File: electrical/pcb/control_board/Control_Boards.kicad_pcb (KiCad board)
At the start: 2 copper layers, 220 x 367.6 mm, 141 parts, among them J1 XT30-M, J10 Molex_172675-0613, J11 Molex_172675-0613, J13 Molex_172675-0613, J14 Molex_172675-0613, J16 277-11404-ND, J17 277-11404-ND, J18 277-11404-ND, J19 TSW-104-07-F-T, J2 ED2580-ND, J20 PEC08SAAN, J21 PPTC102LFBN-RC, J22 S9175-ND_rpi_breakout, J23 S9175-ND_rpi_breakout, J24 6posheader, J25 SSW-104-01-F-T, J26 WM6548-ND, J27 PPTC021LFBN-RC, J28 PPTC021LFBN-RC, J29 PPTC021LFBN-RC, J3 XT30-F, J30 PEC08SAAN, J4 XT30-F, J5 XT30-M, J6 ED2580-ND, J8 Molex_172675-0613, J9 Molex_172675-0613, M1 Mounting_Holes, Q1 2N3906, Q2 2N3906, Q3 2N3906, Q4 2N3906, Q5 2N3906, Q6 2N3906, SW1 CT206124-ND, T1 test_point, T10 test_point, T11 test_point, T12 test_point, T13 test_point, T14 test_point, T15 test_point, T2 test_point, T3 test_point, T4 test_point, T5 test_point, T6 test_point, T7 test_point, T8 test_point, T9 test_point, U1 INA260, U2 PCA9685, U3 D24V22Fx, U4 D24V150Fx, U5 DC7G3HWA, U6 DC7G3HWA, U7 MIC2937A-3.3WT, y1 rover_silkscreen

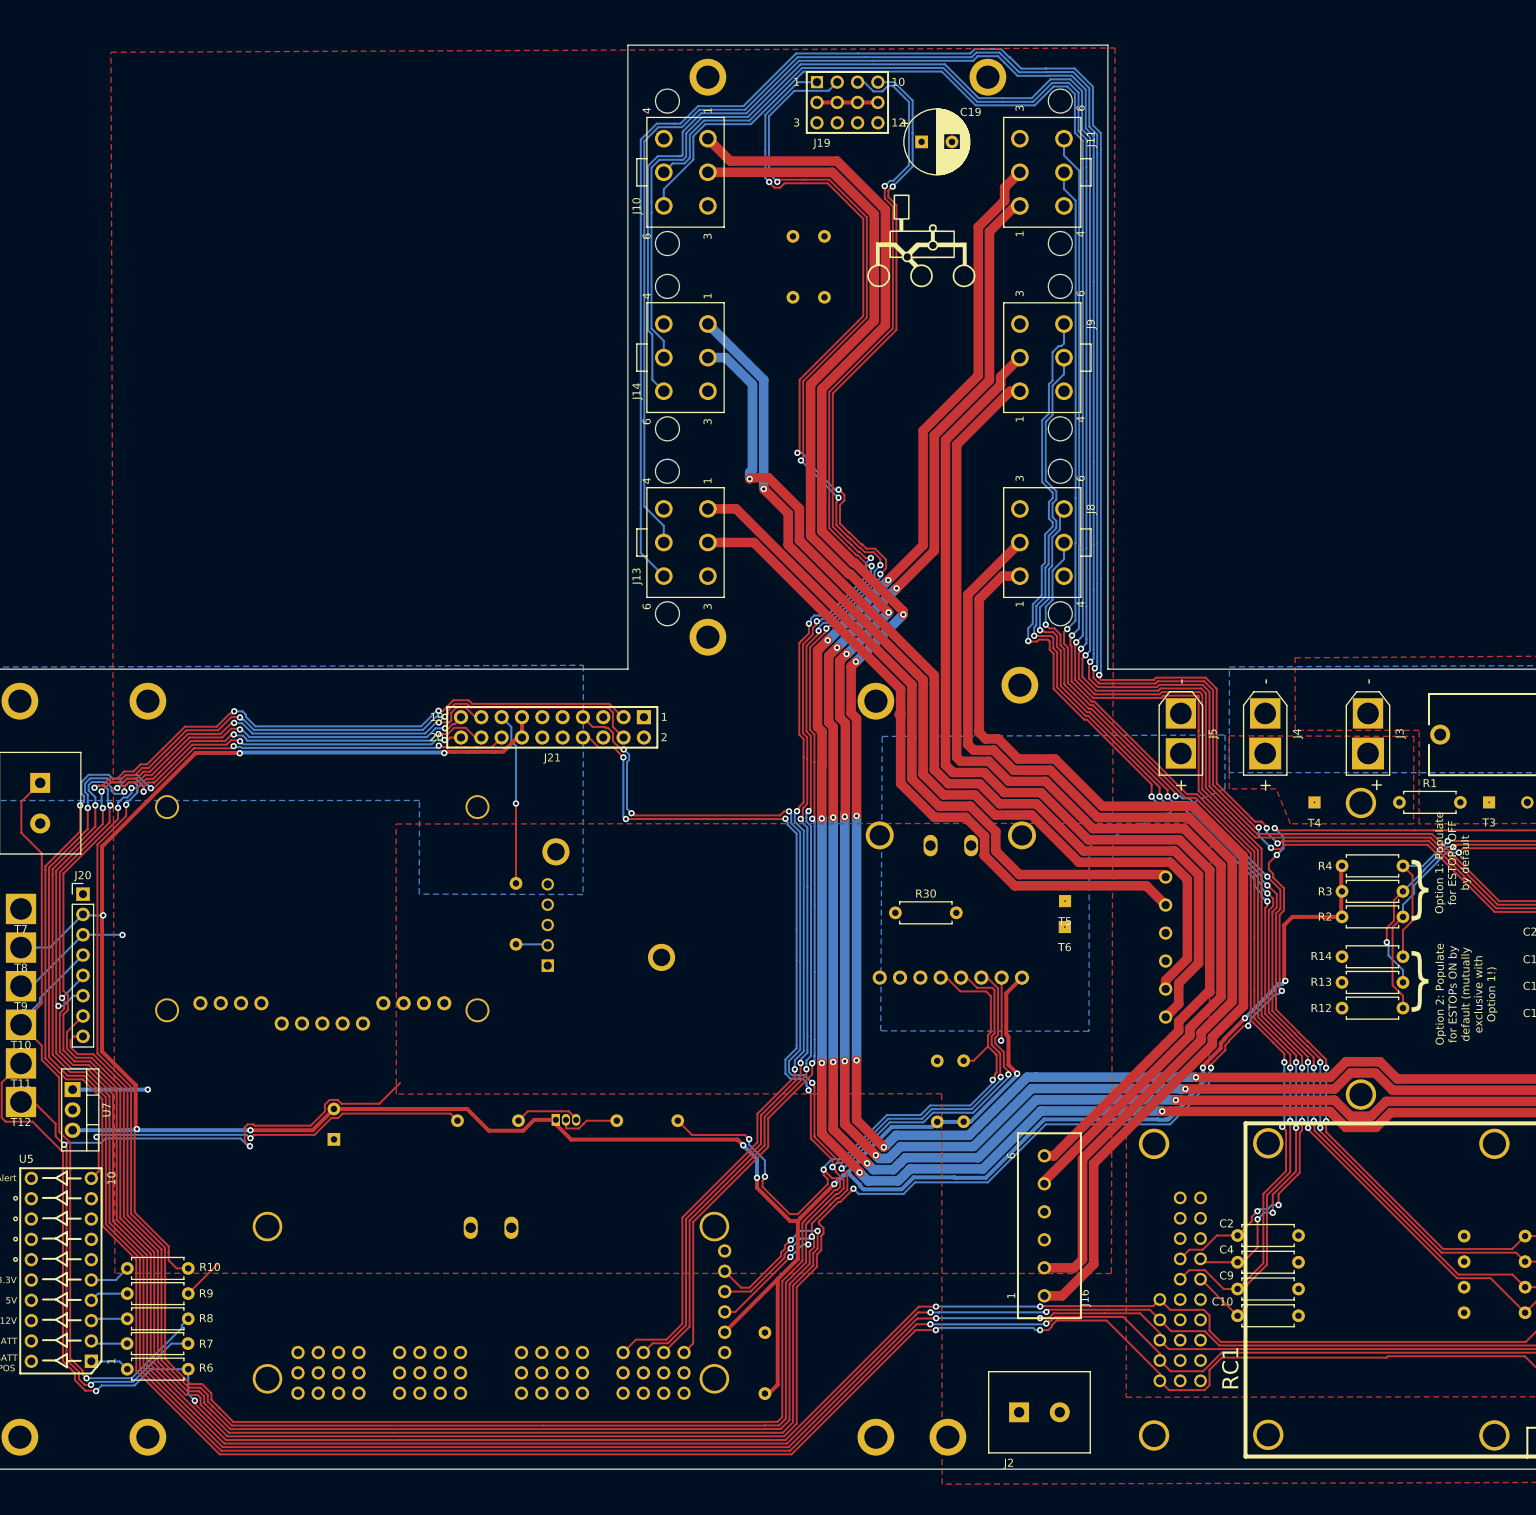
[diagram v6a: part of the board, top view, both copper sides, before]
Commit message: added 2 additional sets of PWM outputs
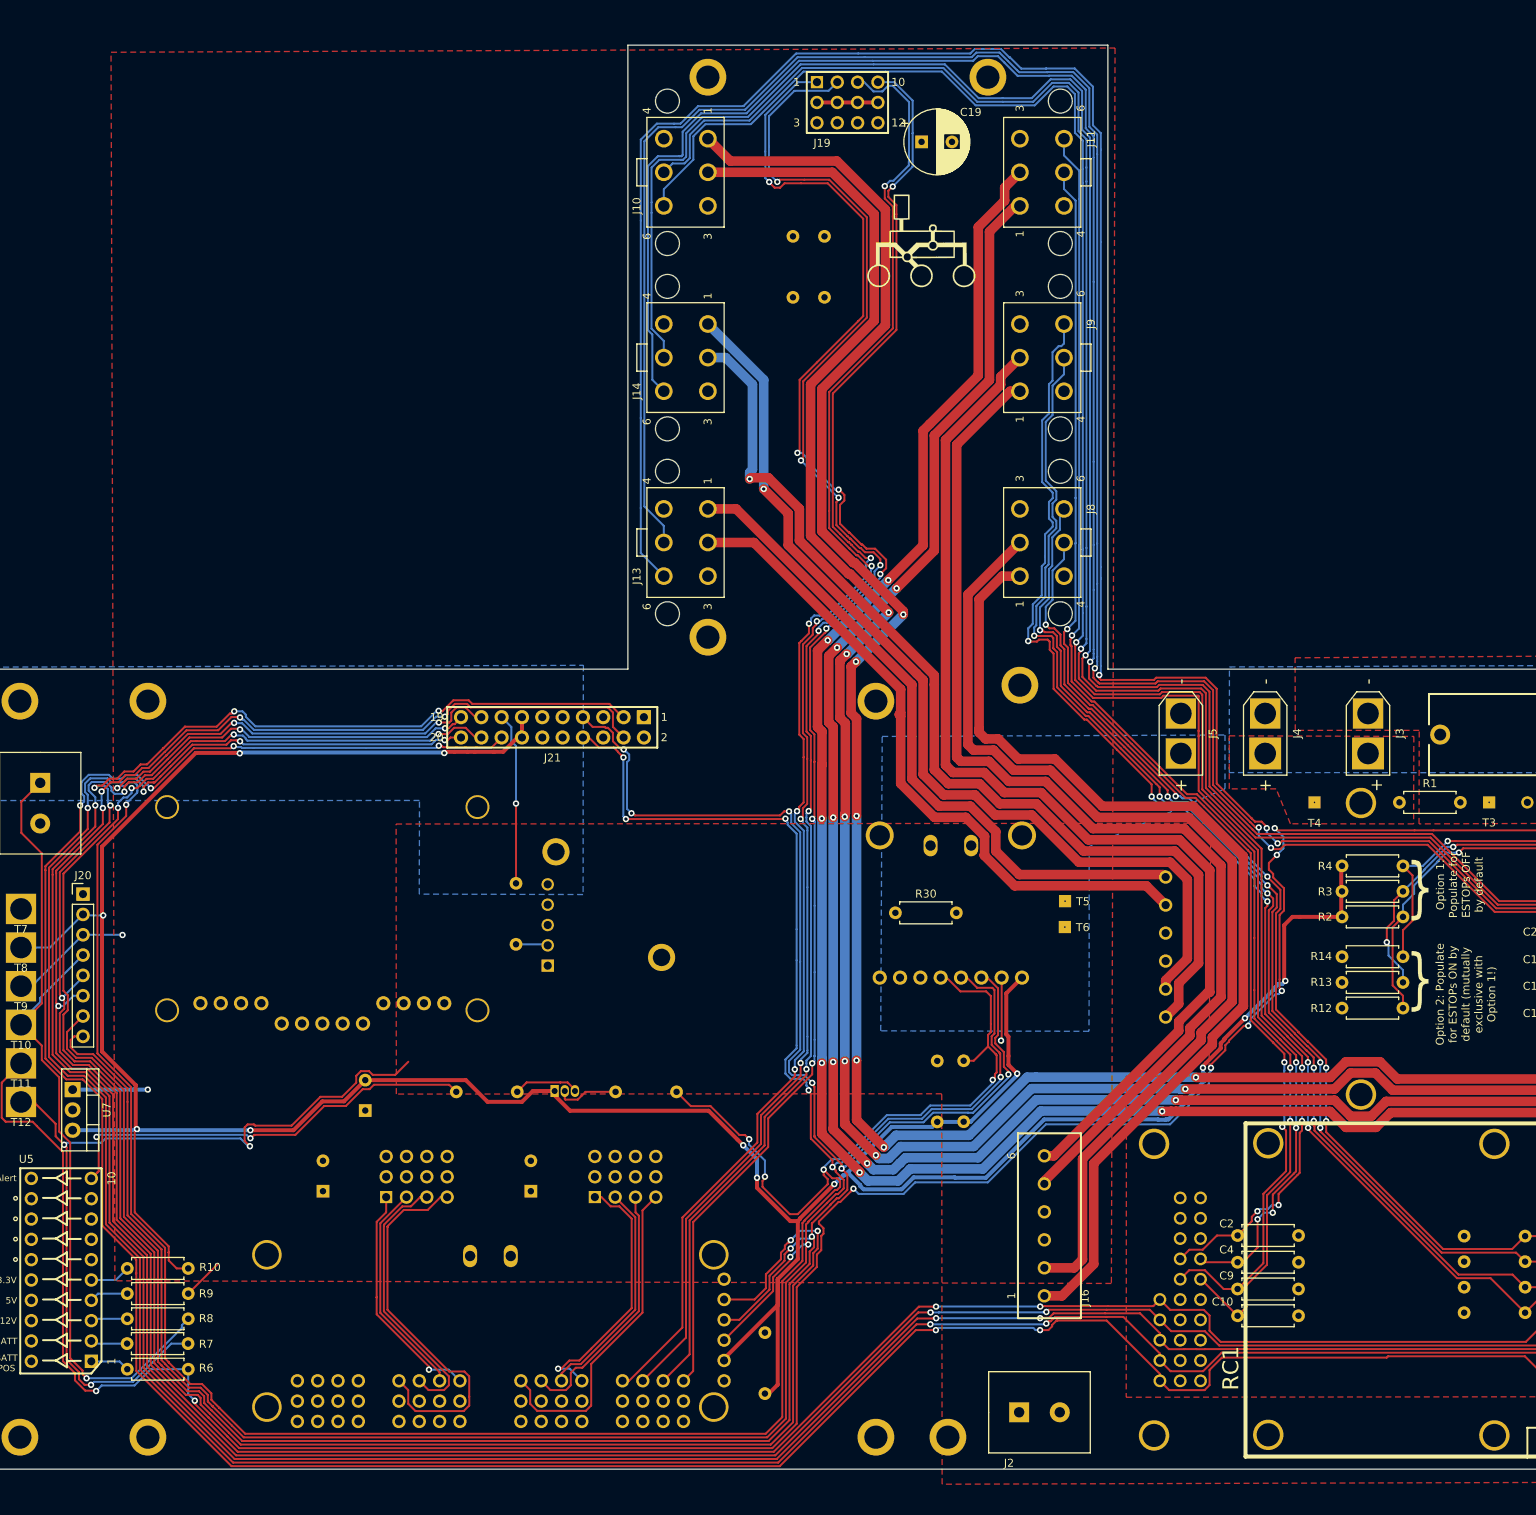
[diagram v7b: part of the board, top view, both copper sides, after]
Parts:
- added C25: 100uf, Capacitor_THT:CP_Radial_D8.0mm_P3.80mm, B.Cu at (67.9, 65.3)
- added C27: 100uf, Capacitor_THT:CP_Radial_D8.0mm_P3.80mm, B.Cu at (41.9, 65.3)
- added J12: TSW-104-07-F-T, JPL Robotics:SSW-104-01-F-T, B.Cu at (49.8, 66.0)
- added J7: TSW-104-07-F-T, JPL Robotics:SSW-104-01-F-T, B.Cu at (75.9, 66.0)
- moved C7 5.32 mm to (47.2, 55.2)
- moved Q1 3.61 mm to (70.8, 52.7)
- moved R15 3.61 mm to (78.5, 52.8)
- moved R24 3.61 mm to (58.5, 52.8)
- moved U2 3.53 mm to (94.1, 95.6)
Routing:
- net /Motor Board/servo_pwm_ch11: track 0.00 -> 48.4 mm
- net /Motor Board/servo_pwm_ch7: track 0.00 -> 41.0 mm
- net /Motor Board/servo_pwm_ch10: track 0.00 -> 34.7 mm
- net /Motor Board/servo_pwm_ch4: track 0.00 -> 32.8 mm, vias 0 -> 1
- net /Motor Board/servo_pwm_ch6: track 0.00 -> 32.1 mm
- net /Motor Board/servo_pwm_ch8: track 0.00 -> 29.2 mm, vias 0 -> 1
- net /Motor Board/servo_pwm_ch5: track 0.00 -> 28.6 mm
- net /Motor Board/servo_pwm_ch9: track 0.00 -> 27.4 mm
- net +3.3V_motor: track 404.7 -> 410.6 mm
- net /Motor Board/SDA_rpi: track 303.4 -> 307.4 mm
- net /Motor Board/SCL_rpi: track 308.1 -> 312.1 mm
- net /Motor Board/servo_pwm_ch0: track 193.8 -> 197.4 mm
- net /Motor Board/servo_pwm_ch1: track 195.3 -> 198.9 mm
- net /Motor Board/alert: track 327.3 -> 330.2 mm
- net /Motor Board/servo_pwm_ch2: track 187.1 -> 189.5 mm
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
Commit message: updating trace thicknesses for J20 and J30
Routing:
- net +12V_brain: track 126.7 -> 124.2 mm, vias 3 -> 4
- net +12V_motor: track 108.8 -> 109.4 mm
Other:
- board text added: "Note: J30 uses thick traces for power lines so that it *could* be used for higher current external applications"
- board text added: "Note: T7 - T12 (large pad test points) and LED signals use thin traces because they don’t need much current. J20 uses thick traces for power lines so that it *could* be used for higher current external applications"
- board text added: "Note: it’s fine that the 5V plane is a little thin up here in the motor connector pandhandle part of the board. Only the corner servos draw their motor current from 5V, whereas the drive motors draw motor current from the roboclaw RC*M*A/B lines. The thinest bit, about 2.5mm, should be more than enough copper to handle the current."
